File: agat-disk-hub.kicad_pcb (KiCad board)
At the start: 2 copper layers, 53.3 x 61 mm, 18 parts, among them J1 IDC‐20, J2 IDC‐20, J3 IDC‐34, J4 IDC‐10, J5 KK‐4

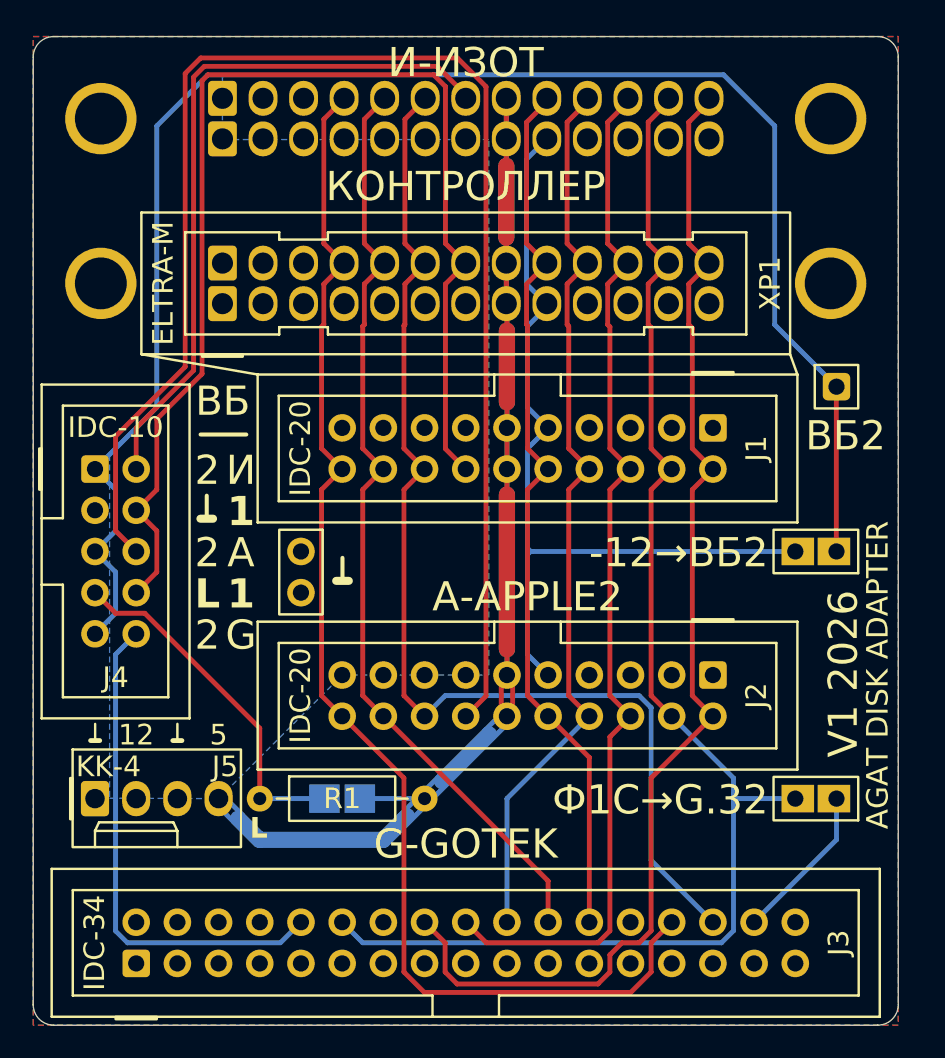
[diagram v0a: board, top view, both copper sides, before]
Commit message: refactor: rename project to agat-disk-hub; add URL to back side; add J5 label
Old project name was agat_disk_adapter.
The permanent URL of the project is now http://museum.computer/re/agat-disk-hub
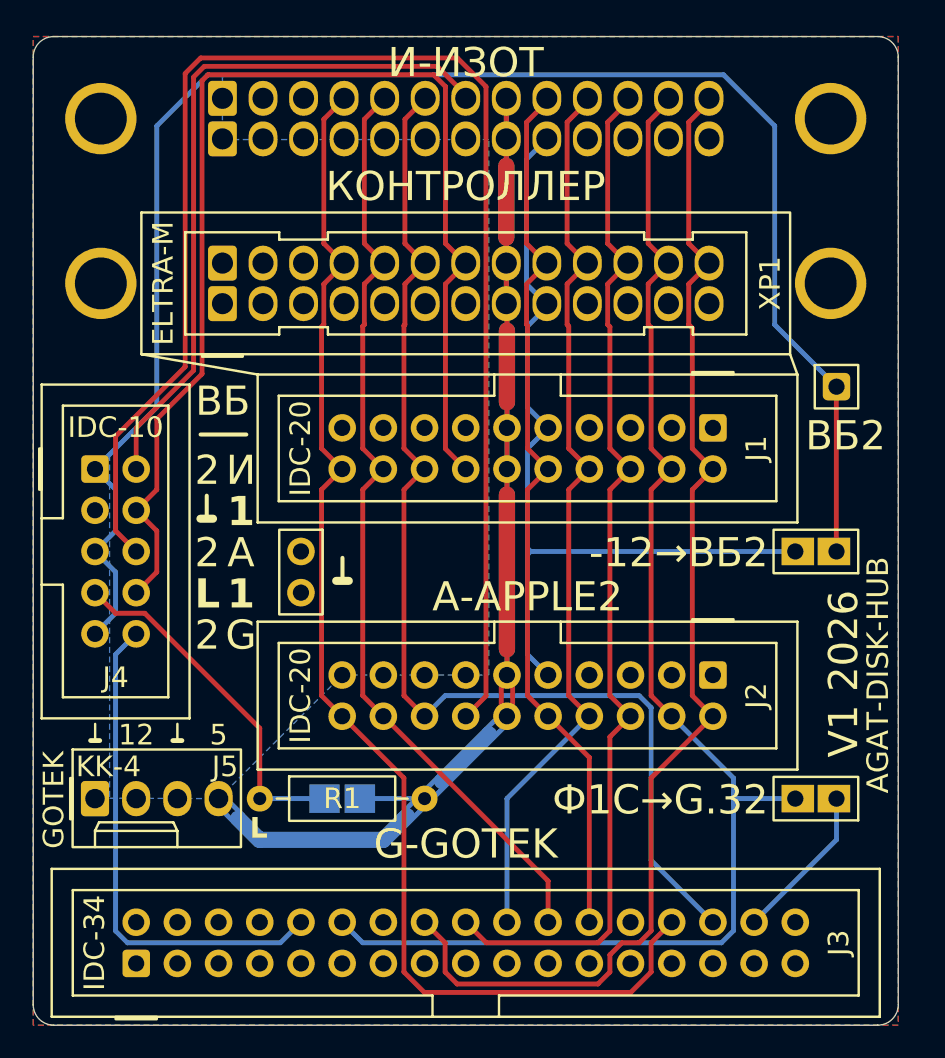
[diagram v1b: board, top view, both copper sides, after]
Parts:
- G*** (x3): footprint agat_disk_adapter:murom_museum_logo_agat_font -> agat-disk-hub:murom_museum_logo_agat_font
- G*** (x2): footprint agat_disk_adapter:AGAT-LOGO-10mm-m-signature -> agat-disk-hub:AGAT-LOGO-10mm-m-signature
- J1, J2: footprint agat_disk_adapter:IDC-20_header_vertical_rotation180 -> agat-disk-hub:IDC-20_header_vertical_rotation180
- J3: footprint agat_disk_adapter:IDC-34_header_vertical_rotation0 -> agat-disk-hub:IDC-34_header_vertical_rotation0
- J4: footprint agat_disk_adapter:IDC-10_header_vertical_rotation270 -> agat-disk-hub:IDC-10_header_vertical_rotation270
- J5: footprint agat_disk_adapter:Molex_KK-4_vertical_rotation0 -> agat-disk-hub:Molex_KK-4_vertical_rotation0
- JP1, JP2: footprint agat_disk_adapter:jumper_pins_solder_drop_vertical -> agat-disk-hub:jumper_pins_solder_drop_vertical
- R2: footprint agat_disk_adapter:jumper_1206_solder_drop -> agat-disk-hub:jumper_1206_solder_drop
- XP1: footprint agat_disk_adapter:Eltra-26M -> agat-disk-hub:Eltra-26M
- XS1: footprint agat_disk_adapter:Eltra-26F -> agat-disk-hub:Eltra-26F
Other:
- board text added: "AGAT-DISK-HUB"
- board text added: "GOTEK"
- board text added: "MUSEUM.COMPUTER/RE/AGAT-DSK-HUB"
- board text removed: "AGAT DISK ADAPTER"
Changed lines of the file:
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@@
 	(paper "A5" portrait)
 	(title_block
-		(title "AGAT DISK ADAPTER")
+		(title "AGAT DISK HUB")
 		(date "2026-09")
 		(rev "V1")
@@
 		)
 	)
-	(footprint "agat_disk_adapter:murom_museum_logo_agat_font"
+	(footprint "agat-disk-hub:murom_museum_logo_agat_font"
 		(layer "F.Cu")
 		(at 51.92 58.88)
@@
 		(embedded_fonts no)
 	)
-	(footprint "agat_disk_adapter:Molex_KK-4_vertical_rotation0"
+	(footprint "agat-disk-hub:Molex_KK-4_vertical_rotation0"
 		(layer "F.Cu")
 		(at 50.72 104.36)
@@
 		(property ki_fp_filters "Connector*:*_1x??_*")
 		(sheetname "/")
-		(sheetfile "agat_disk_adapter.kicad_sch")
+		(sheetfile "agat-disk-hub.kicad_sch")
 		(units
 			(unit
@@
 		)
 	)
-	(footprint "agat_disk_adapter:murom_museum_logo_agat_font"
+	(footprint "agat-disk-hub:murom_museum_logo_agat_font"
 		(layer "F.Cu")
 		(at 51.67 65.985)
@@
 		(embedded_fonts no)
 	)
-	(footprint "agat_disk_adapter:IDC-34_header_vertical_rotation0"
+	(footprint "agat-disk-hub:IDC-34_header_vertical_rotation0"
 		(layer "F.Cu")
 		(at 53.26 114.52)
@@
 		(property ki_fp_filters "Connector*:*_2x??_*")
 		(sheetname "/")
-		(sheetfile "agat_disk_adapter.kicad_sch")
+		(sheetfile "agat-disk-hub.kicad_sch")
 		(units
 			(unit
@@
 		(property ki_fp_filters "R_*")
 		(sheetname "/")
-		(sheetfile "agat_disk_adapter.kicad_sch")
+		(sheetfile "agat-disk-hub.kicad_sch")
 		(units
 			(unit
@@
 		)
 	)
-	(footprint "agat_disk_adapter:AGAT-LOGO-10mm-m-signature"
+	(footprint "agat-disk-hub:AGAT-LOGO-10mm-m-signature"
 		(layer "F.Cu")
 		(at 94.86 66.46)
@@
 		(embedded_fonts no)
 	)
-	(footprint "agat_disk_adapter:IDC-10_header_vertical_rotation270"
+	(footprint "agat-disk-hub:IDC-10_header_vertical_rotation270"
 		(layer "F.Cu")
 		(at 50.72 84.04)
@@
 		(property ki_fp_filters "Connector*:*_2x??_*")
 		(sheetname "/")
-		(sheetfile "agat_disk_adapter.kicad_sch")
+		(sheetfile "agat-disk-hub.kicad_sch")
 		(units
 			(unit
@@
 		)
 	)
-	(footprint "agat_disk_adapter:IDC-20_header_vertical_rotation180"
+	(footprint "agat-disk-hub:IDC-20_header_vertical_rotation180"
 		(layer "F.Cu")
 		(at 88.82 96.74)
@@
 		(property ki_fp_filters "Connector*:*_2x??_*")
 		(sheetname "/")
-		(sheetfile "agat_disk_adapter.kicad_sch")
+		(sheetfile "agat-disk-hub.kicad_sch")
 		(units
 			(unit
@@
 		)
 	)
-	(footprint "agat_disk_adapter:IDC-20_header_vertical_rotation180"
+	(footprint "agat-disk-hub:IDC-20_header_vertical_rotation180"
 		(layer "F.Cu")
 		(at 88.82 81.5)
@@
 		(property ki_fp_filters "Connector*:*_2x??_*")
 		(sheetname "/")
-		(sheetfile "agat_disk_adapter.kicad_sch")
+		(sheetfile "agat-disk-hub.kicad_sch")
 		(units
 			(unit
@@
 		(tags "Through hole pin header THT 1x01 2.00mm single row")
 		(property "Reference" "XT1"
-			(at 0 -2.41 0)
+			(at 1.23 -2.41 0)
 			(unlocked yes)
 			(layer "B.SilkS")
@@
 					(thickness 0.25)
 				)
-				(justify mirror)
+				(justify left mirror)
 			)
 		)
@@
 		(property ki_fp_filters "Connector*:*_1x??_*")
 		(sheetname "/")
-		(sheetfile "agat_disk_adapter.kicad_sch")
+		(sheetfile "agat-disk-hub.kicad_sch")
 		(units
 			(unit
@@
 		)
 	)
-	(footprint "agat_disk_adapter:jumper_pins_solder_drop_vertical"
+	(footprint "agat-disk-hub:jumper_pins_solder_drop_vertical"
 		(layer "F.Cu")
 		(at 96.44 89.12 180)
@@
 		(tags "Through hole pin header THT 1x02 2.54mm")
 		(property "Reference" "JP1"
-			(at 1.27 2.3 0)
+			(at -1.23 2.3 0)
 			(layer "B.SilkS")
 			(effects
@@
 					(thickness 0.25)
 				)
-				(justify mirror)
+				(justify left mirror)
 			)
 		)
@@
 		(property ki_fp_filters "Connector*:*_1x??_*")
 		(sheetname "/")
-		(sheetfile "agat_disk_adapter.kicad_sch")
+		(sheetfile "agat-disk-hub.kicad_sch")
 		(units
 			(unit
@@
 		(property ki_fp_filters "Connector*:*_1x??_*")
 		(sheetname "/")
-		(sheetfile "agat_disk_adapter.kicad_sch")
+		(sheetfile "agat-disk-hub.kicad_sch")
 		(units
 			(unit
@@
 		)
 	)
-	(footprint "agat_disk_adapter:murom_museum_logo_agat_font"
+	(footprint "agat-disk-hub:murom_museum_logo_agat_font"
 		(layer "F.Cu")
 		(at 95.24 58.88)
@@
 		(embedded_fonts no)
 	)
-	(footprint "agat_disk_adapter:Eltra-26M"
+	(footprint "agat-disk-hub:Eltra-26M"
 		(layer "F.Cu")
 		(at 73.58 71.34)
@@
 		)
 		(sheetname "/")
-		(sheetfile "agat_disk_adapter.kicad_sch")
+		(sheetfile "agat-disk-hub.kicad_sch")
 		(units
 			(unit
@@
 		)
 	)
-	(footprint "agat_disk_adapter:jumper_pins_solder_drop_vertical"
+	(footprint "agat-disk-hub:jumper_pins_solder_drop_vertical"
 		(layer "F.Cu")
 		(at 96.44 104.36 180)
@@
 		(tags "Through hole pin header THT 1x02 2.54mm")
 		(property "Reference" "JP2"
-			(at 1.27 2.41 0)
+			(at -1.23 2.41 0)
 			(layer "B.SilkS")
 			(effects
@@
 					(thickness 0.25)
 				)
-				(justify mirror)
+				(justify left mirror)
 			)
 		)
@@
 		(property ki_fp_filters "Connector*:*_1x??_*")
 		(sheetname "/")
-		(sheetfile "agat_disk_adapter.kicad_sch")
+		(sheetfile "agat-disk-hub.kicad_sch")
 		(units
 			(unit
@@
 		)
 	)
-	(footprint "agat_disk_adapter:jumper_1206_solder_drop"
+	(footprint "agat-disk-hub:jumper_1206_solder_drop"
 		(layer "B.Cu")
 		(at 65.96 104.36 180)
@@
 		(property ki_fp_filters "R_*")
 		(sheetname "/")
-		(sheetfile "agat_disk_adapter.kicad_sch")
+		(sheetfile "agat-disk-hub.kicad_sch")
 		(units
 			(unit
@@
 		)
 	)
-	(footprint "agat_disk_adapter:Eltra-26F"
+	(footprint "agat-disk-hub:Eltra-26F"
 		(layer "B.Cu")
 		(at 73.58 61.18 180)
@@
 		)
 		(sheetname "/")
-		(sheetfile "agat_disk_adapter.kicad_sch")
+		(sheetfile "agat-disk-hub.kicad_sch")
 		(units
 			(unit
@@
 		)
 	)
-	(footprint "agat_disk_adapter:AGAT-LOGO-10mm-m-signature"
+	(footprint "agat-disk-hub:AGAT-LOGO-10mm-m-signature"
 		(layer "B.Cu")
 		(at 52.318611 97.88 180)
@@
 		)
 	)
-	(gr_text "AGAT DISK ADAPTER"
-		(at 98.2 96.74 90)
+	(gr_text "GOTEK"
+		(at 48.92 104.44 90)
+		(layer "F.SilkS")
+		(effects
+			(font
+				(size 1.27 1.27)
+				(thickness 0.15)
+			)
+			(justify bottom)
+		)
+	)
+	(gr_text "AGAT-DISK-HUB"
+		(at 98.22 96.74 90)
 		(layer "F.SilkS" knockout)
 		(effects
@@
 	)
 	(gr_text "V1 2026"
-		(at 96.86 96.66 90)
+		(at 96.88 96.66 90)
 		(layer "F.SilkS" knockout)
 		(effects
@@
 		)
 	)
+	(gr_text "DE2"
+		(at 97.67 80.74 0)
+		(layer "B.SilkS")
+		(effects
+			(font
+				(size 1.27 1.27)
+				(thickness 0.15)
+				(bold yes)
+			)
+			(justify left mirror)
+		)
+	)
 	(gr_text "GND"
 		(at 50.72 107.93 0)
@@
 		)
 	)
-	(gr_text "DE2"
-		(at 96.44 80.75 0)
-		(layer "B.SilkS")
-		(effects
-			(font
-				(size 1.27 1.27)
-				(thickness 0.15)
-				(bold yes)
-			)
-			(justify mirror)
-		)
-	)
 	(gr_text "+12"
 		(at 69.77 80.54 0)
@@
 		)
 	)
+	(gr_text "MUSEUM.COMPUTER/RE/AGAT-DSK-HUB"
+		(at 98.81 117.26 270)
+		(layer "B.SilkS" knockout)
+		(effects
+			(font
+				(size 1.33 1.33)
+				(thickness 0.2)
+			)
+			(justify left mirror)
+		)
+	)
